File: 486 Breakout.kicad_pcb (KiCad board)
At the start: 4 copper layers, 100 x 100 mm, 51 parts, among them J1 PWR, J10 Conn_02x03_Counter_Clockwise, J11 Cache FPU, J12 Parity, J13 Bus Size Byte Enabled, J14 Bus Arbitration, J2 Not Connected, J3 Address Bus, J4 Data Bus, J5 CLK, J6 Conn_02x03_Counter_Clockwise, J7 Int, J8 Control Bus, J9 Conn_02x04_Counter_Clockwise, SW1 POWER, SW2 RESET, U1 80486, U2 7400, U3 7400

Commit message: V2 of the board
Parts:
- removed G***: LOGO, Private_lib:Fox Logo
- removed the J7 at (165.6, 117.6)
- removed the R20 at (157.8, 119.1)
- removed SW1: POWER, Button_Switch_THT:SW_NKK_G1xJP
- removed SW2: RESET, Button_Switch_THT:SW_PUSH_6mm_H5mm
- added #LOGO1: LOGO, Private_lib:Fox Logo, F.Cu at (157.2, 133.3)
- added J12: FPU, Connector_PinHeader_2.54mm:PinHeader_1x02_P2.54mm_Vertical, F.Cu at (74.9, 124.7)
- added J14: Bus Size, Connector_PinHeader_2.54mm:PinHeader_1x02_P2.54mm_Vertical, F.Cu at (74.4, 75.4)
- added R14: 10k, Resistor_THT:R_Axial_DIN0204_L3.6mm_D1.6mm_P7.62mm_Horizontal, F.Cu at (158.8, 77.0)
- C1, C10, C2, C3, C4, C5, C6, C7, C8, C9: value C -> 105
- D1: value LED_ALT -> POWER
- J11: renamed from J13; value Bus Size Byte Enabled -> Byte Enabled; footprint Connector_PinHeader_2.54mm:PinHeader_1x08_P2.54mm_Vertical -> Connector_PinHeader_2.54mm:PinHeader_1x06_P2.54mm_Vertical
- J13: renamed from J5; value CLK -> Input; footprint Connector_PinHeader_2.54mm:PinHeader_1x01_P2.54mm_Vertical -> Connector_PinHeader_2.54mm:PinHeader_1x04_P2.54mm_Vertical
- J7: renamed from J8; footprint Connector_PinHeader_2.54mm:PinHeader_1x10_P2.54mm_Vertical -> Connector_PinHeader_2.54mm:PinHeader_1x09_P2.54mm_Vertical
- J8: renamed from J11; value Cache FPU -> Cache; footprint Connector_PinHeader_2.54mm:PinHeader_1x08_P2.54mm_Vertical -> Connector_PinHeader_2.54mm:PinHeader_1x06_P2.54mm_Vertical
- R1: footprint Resistor_THT:R_Axial_DIN0204_L3.6mm_D1.6mm_P5.08mm_Horizontal -> Resistor_THT:R_Axial_DIN0204_L3.6mm_D1.6mm_P7.62mm_Horizontal
- R10: renamed from R12; footprint Resistor_THT:R_Axial_DIN0204_L3.6mm_D1.6mm_P5.08mm_Horizontal -> Resistor_THT:R_Axial_DIN0204_L3.6mm_D1.6mm_P7.62mm_Horizontal
- R11: renamed from R13; footprint Resistor_THT:R_Axial_DIN0204_L3.6mm_D1.6mm_P5.08mm_Horizontal -> Resistor_THT:R_Axial_DIN0204_L3.6mm_D1.6mm_P7.62mm_Horizontal
- R12: renamed from R14; footprint Resistor_THT:R_Axial_DIN0204_L3.6mm_D1.6mm_P5.08mm_Horizontal -> Resistor_THT:R_Axial_DIN0204_L3.6mm_D1.6mm_P7.62mm_Horizontal
- R13: renamed from R15; footprint Resistor_THT:R_Axial_DIN0204_L3.6mm_D1.6mm_P5.08mm_Horizontal -> Resistor_THT:R_Axial_DIN0204_L3.6mm_D1.6mm_P7.62mm_Horizontal
- R15: renamed from R16; footprint Resistor_THT:R_Axial_DIN0204_L3.6mm_D1.6mm_P5.08mm_Horizontal -> Resistor_THT:R_Axial_DIN0204_L3.6mm_D1.6mm_P7.62mm_Horizontal
- R16: renamed from R17; footprint Resistor_THT:R_Axial_DIN0204_L3.6mm_D1.6mm_P5.08mm_Horizontal -> Resistor_THT:R_Axial_DIN0204_L3.6mm_D1.6mm_P7.62mm_Horizontal
- R17: renamed from R18; footprint Resistor_THT:R_Axial_DIN0204_L3.6mm_D1.6mm_P5.08mm_Horizontal -> Resistor_THT:R_Axial_DIN0204_L3.6mm_D1.6mm_P7.62mm_Horizontal
- R18: renamed from R19; footprint Resistor_THT:R_Axial_DIN0204_L3.6mm_D1.6mm_P5.08mm_Horizontal -> Resistor_THT:R_Axial_DIN0204_L3.6mm_D1.6mm_P7.62mm_Horizontal
- R19: renamed from R2; footprint Resistor_THT:R_Axial_DIN0204_L3.6mm_D1.6mm_P5.08mm_Horizontal -> Resistor_THT:R_Axial_DIN0204_L3.6mm_D1.6mm_P7.62mm_Horizontal
- R2: renamed from R4; footprint Resistor_THT:R_Axial_DIN0204_L3.6mm_D1.6mm_P5.08mm_Horizontal -> Resistor_THT:R_Axial_DIN0204_L3.6mm_D1.6mm_P7.62mm_Horizontal
- R20: renamed from R3; footprint Resistor_THT:R_Axial_DIN0204_L3.6mm_D1.6mm_P5.08mm_Horizontal -> Resistor_THT:R_Axial_DIN0204_L3.6mm_D1.6mm_P7.62mm_Horizontal
- R3: renamed from R5; footprint Resistor_THT:R_Axial_DIN0204_L3.6mm_D1.6mm_P5.08mm_Horizontal -> Resistor_THT:R_Axial_DIN0204_L3.6mm_D1.6mm_P7.62mm_Horizontal
- R4: renamed from R6; footprint Resistor_THT:R_Axial_DIN0204_L3.6mm_D1.6mm_P5.08mm_Horizontal -> Resistor_THT:R_Axial_DIN0204_L3.6mm_D1.6mm_P7.62mm_Horizontal
- R5: renamed from R7; footprint Resistor_THT:R_Axial_DIN0204_L3.6mm_D1.6mm_P5.08mm_Horizontal -> Resistor_THT:R_Axial_DIN0204_L3.6mm_D1.6mm_P7.62mm_Horizontal
- R6: renamed from R8; footprint Resistor_THT:R_Axial_DIN0204_L3.6mm_D1.6mm_P5.08mm_Horizontal -> Resistor_THT:R_Axial_DIN0204_L3.6mm_D1.6mm_P7.62mm_Horizontal
- R7: renamed from R9; footprint Resistor_THT:R_Axial_DIN0204_L3.6mm_D1.6mm_P5.08mm_Horizontal -> Resistor_THT:R_Axial_DIN0204_L3.6mm_D1.6mm_P7.62mm_Horizontal
- R8: renamed from R10; footprint Resistor_THT:R_Axial_DIN0204_L3.6mm_D1.6mm_P5.08mm_Horizontal -> Resistor_THT:R_Axial_DIN0204_L3.6mm_D1.6mm_P7.62mm_Horizontal
- R9: renamed from R11; footprint Resistor_THT:R_Axial_DIN0204_L3.6mm_D1.6mm_P5.08mm_Horizontal -> Resistor_THT:R_Axial_DIN0204_L3.6mm_D1.6mm_P7.62mm_Horizontal
- U1: value 80486 -> 80486DX
- moved J6 42.6 mm to (87.9, 117.8), turned to 0 degrees
- moved J10 37.7 mm to (158.0, 97.0)
- moved R11 31.1 mm to (158.8, 73.9)
- moved R7 29.0 mm to (89.4, 140.2)
- moved R1 28.5 mm to (158.8, 70.9)
- moved R17 27.6 mm to (158.8, 83.1)
- moved C10 27.2 mm to (130.8, 124.7)
- moved U3 27.2 mm to (119.4, 124.7)
- moved R2 24.4 mm to (80.3, 81.8), turned to 180 degrees
- moved R19 24.3 mm to (158.8, 89.2)
- moved R20 24.1 mm to (158.8, 92.2)
- moved R6 23.7 mm to (89.4, 137.7)
- moved R16 22.2 mm to (158.8, 80.0)
- moved R18 21.7 mm to (158.8, 86.1)
- moved R5 18.4 mm to (89.4, 135.1)
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- renumbered J14 to J15, J9 to J2, J2 to J3, J3 to J4, J4 to J5, J12 to J9
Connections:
- net /RDY*R renamed /RDY#R
- net ADS* renamed ADS#
- net BE0* renamed BE0#
- net BE1* renamed BE1#
- net BE2* renamed BE2#
- net BE3* renamed BE3#
- net BLAST* renamed BLAST#
- net BOFF* renamed BOFF#
- net D_C* renamed D_C#
- net EADS* renamed EADS#
- net FERR* renamed FERR#
- net FLUSH* renamed FLUSH#
- net LOCK* renamed LOCK#
- net M_IO* renamed M_IO#
- net PCHK* renamed PCHK#
- net PLOCK* renamed PLOCK#
- net RDY* renamed RDY#
- net W_R* renamed W_R#
- J1 pad 1: Net-(J1-Pad1) -> +5V
- J10 pad 4: /BRDY*R -> /BRDY#R
- J2 pad 2: Net-(J9-Pad2) -> Net-(J2-Pad2)
- J2 pad 4: Net-(J9-Pad4) -> Net-(J2-Pad4)
- J2 pad 6: Net-(J9-Pad6) -> Net-(J2-Pad6)
- J2 pad 8: Net-(J9-Pad8) -> Net-(J2-Pad8)
- J6 pad 1: A20M* -> A20M#
- J6 pad 3: KEN* -> KEN#
- J6 pad 5: IGNNE* -> IGNNE#
- J7 pad 6: BRDY* -> BRDY#
- J8 pad 1: IGNNE* -> IGNNE#
- J8 pad 5: KEN* -> KEN#
- R12 pad 1: BS16* -> BS8#
- R13 pad 1: BS8* -> BS16#
- R17 pad 1: NMI -> INTR
- R18 pad 1: INTR -> NMI
- R2 pad 1: KEN* -> A20M#
- R20 pad 1: /BRDY*R -> BRDY#
- R20 pad 2: BRDY* -> /BRDY#R
- R3 pad 1: A20M* -> IGNNE#
- R4 pad 1: Net-(J9-Pad8) -> Net-(J2-Pad2)
- R5 pad 1: Net-(J9-Pad6) -> Net-(J2-Pad4)
- R6 pad 1: Net-(J9-Pad4) -> Net-(J2-Pad6)
- R7 pad 1: Net-(J9-Pad2) -> Net-(J2-Pad8)
- R9 pad 1: IGNNE* -> KEN#
- U1 pad A15: IGNNE* -> IGNNE#
- U1 pad C17: BS16* -> BS16#
- U1 pad D15: A20M* -> A20M#
- U1 pad D16: BS8* -> BS8#
- U1 pad F15: KEN* -> KEN#
- U1 pad H15: BRDY* -> BRDY#
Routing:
- net IGNNE*: track 139.2 -> 0.00 mm
- net A24: track 210.1 -> 72.5 mm, vias 2 -> 1
- net KEN#: track 0.00 -> 119.4 mm
- net KEN*: track 115.1 -> 0.00 mm, vias 2 -> 0
- net A20M#: track 0.00 -> 114.8 mm, vias 0 -> 3
- net BRDY*: track 109.0 -> 0.00 mm
- net A20M*: track 107.7 -> 0.00 mm, vias 2 -> 0
- net A30: track 77.6 -> 170.7 mm, vias 1 -> 3
- net IGNNE#: track 0.00 -> 86.1 mm
- net A29: track 193.8 -> 110.0 mm
- net A18: track 133.4 -> 52.8 mm, vias 2 -> 0
- net LOCK#: track 41.1 -> 109.9 mm, vias 0 -> 1
- net BS8#: track 0.00 -> 67.5 mm
- net BS16#: track 0.00 -> 64.5 mm
- net A28: track 90.3 -> 152.6 mm
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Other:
- board text added: "486-DX Breakout Board V2.0 Created by Fox Cutter"
- board text added: "A0 is valid when ~BS8~ is asserted."
- board text added: "A1 is valid when ~BS8~ or ~BS16~ are asserted."
- board text added: "A15"
- board text added: "A23"
- board text added: "A3 (TCK) A10 A12 A13 A14 (TDI) B10 B12 B13 B14 (TMS) B16 (TDO) C10 C11 (~UP~) C12 C13 G15 R17 S4"
- board text added: "A7"
- board text added: "AHOLD ~EADS ~KEN ~FLUSH PWT PCD"
- board text added: "BREQ HOLD HLDA ~BOFF"
- board text added: "CLK RESET INTR NMI"
- board text added: "D15"
- board text added: "D23"
- board text added: "D7"
- board text added: "DP0 DP1 DP2 DP3 ~PCHK"
- board text added: "M/~IO D/~C W/~R ~ADS ~RDY ~BRDY ~BLAST ~LOCK ~PLOCK"
- board text added: "Pull Low Pull High"
- board text added: "when ~BS16~ is asserted."
- board text added: "~A20M ~KEN ~IGNNE"
- board text added: "~BE0 ~BE1 ~BE2 ~BE3 ~BLE ~BHE"
- board text added: "~BHE~ and ~BLE~ are valid"
- board text added: "~BS8 ~BS16"
- board text added: "~IGNNE ~FERR"
- board text added: "~RDY ~BRDY"
- board text removed: "486-DX Breakout Board V1.0 Created by Fox Cutter"
- board text removed: "A0 is valid when BS8# is asserted. A1 is valid when BS8# or BS16# are asserted."
- board text removed: "A3 (TCK) A10 A12 A13 A14 (TDI) B10 B12 B13 B14 (TMS) B16 (TDO) C10 C11 (UP#) C12 C13 G15 R17 S4"
- board text removed: "BE0# BE1# BE2# BE3# BLE# BHE# BS8# BS16#"
- board text removed: "BHE# and BLE# are valid when BS16# is asserted."
- board text removed: "BREQ HOLD HLDA BOFF#"
- board text removed: "DP0 DP1 DP2 DP3 PCHK#"
- board text removed: "IGNNE# FERR# AHOLD EADS# KEN# FLUSH# PWT PCD"
- board text removed: "IGNNE# KEN# A20M#"
- board text removed: "INTR NMI"
- board text removed: "M/IO# D/C# W/R# ADS# RDY# BRDY# BLAST# LOCK# PLOCK# RESET"
- board text removed: "Pull Low Float Pull High"
- board text removed: "RDY# BRDY#"
- board text removed: "ZIF Socket"

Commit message: * Update to Kicad 6
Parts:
- J13: footprint Connector_PinHeader_2.54mm:PinHeader_1x04_P2.54mm_Vertical -> Connector_PinHeader_2.54mm:PinHeader_1x06_P2.54mm_Vertical
- J7: footprint Connector_PinHeader_2.54mm:PinHeader_1x09_P2.54mm_Vertical -> Connector_PinHeader_2.54mm:PinHeader_1x07_P2.54mm_Vertical
- U1: footprint 486:PGA169 -> 486 Breakout:PGA169
- moved J10 19.4 mm to (158.1, 77.7)
- moved R11 17.1 mm to (158.4, 91.0)
- moved R14 17.1 mm to (158.4, 94.1)
- moved R16 17.1 mm to (158.4, 97.1)
- moved R17 17.1 mm to (158.4, 100.2)
- moved R18 17.1 mm to (158.4, 103.2)
- moved R19 17.1 mm to (158.4, 106.3)
- moved R20 17.1 mm to (158.4, 109.3)
- moved U2 6.67 mm to (110.3, 124.9)
- moved U3 6.67 mm to (126.1, 124.9)
- moved C10 6.67 mm to (137.5, 124.9)
- moved C9 6.67 mm to (121.5, 124.9)
- moved J7 3.59 mm to (165.7, 90.3)
- moved J6 2.17 mm to (88.0, 115.7)
- moved J15 1.90 mm to (165.7, 110.5)
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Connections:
- J12 pad 1: PWT -> IGNNE#
- J12 pad 2: PCD -> FERR#
- J13 pad 3: INTR -> RDY#
- J13 pad 4: NMI -> BRDY#
- J7 pad 5: RDY# -> BLAST#
- J7 pad 6: BRDY# -> LOCK#
- J7 pad 7: BLAST# -> PLOCK#
- J8 pad 1: IGNNE# -> AHOLD
- J8 pad 2: FERR# -> EADS#
- J8 pad 3: AHOLD -> KEN#
- J8 pad 4: EADS# -> FLUSH#
- J8 pad 5: KEN# -> PWT
- J8 pad 6: FLUSH# -> PCD
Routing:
- net A31: track 189.7 -> 92.8 mm
- net A27: track 77.3 -> 165.1 mm, vias 0 -> 1
- net A30: track 170.7 -> 90.9 mm, vias 3 -> 0
- net NMI: track 68.1 -> 133.4 mm, vias 0 -> 8
- net A11: track 93.1 -> 28.3 mm, vias 5 -> 2
- net A18: track 52.8 -> 115.2 mm, vias 0 -> 6
- net INTR: track 71.9 -> 133.8 mm, vias 0 -> 3
- net A26: track 79.1 -> 139.1 mm, vias 0 -> 3
- net A9: track 40.0 -> 99.8 mm, vias 2 -> 11
- net A23: track 76.3 -> 132.7 mm, vias 2 -> 5
- net D10: track 55.6 -> 108.7 mm
- net LOCK#: track 109.9 -> 57.8 mm, vias 1 -> 2
- net NC1: track 33.0 -> 85.0 mm, vias 0 -> 2
- net A5: track 31.2 -> 82.3 mm, vias 1 -> 5
- net A29: track 110.0 -> 160.9 mm, vias 1 -> 6
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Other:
- net class +5V removed
- net class Default removed
- net class GND removed
- board text added: "A0 is valid when ~{BS8} is asserted."
- board text added: "A1 is valid when ~{BS8} or ~{BS16} are asserted."
- board text added: "A3 (TCK) A10 A12 A13 A14 (TDI) B10 B12 B13 B14 (TMS) B16 (TDO) C10 C11 (~{UP}) C12 C13 G15 R17 S4"
- board text added: "AHOLD ~{EADS} ~{KEN} ~{FLUSH} PWT PCD"
- board text added: "BREQ HOLD HLDA ~{BOFF}"
- board text added: "CLK RESET ~{RDY} ~{BRDY} INTR NMI"
- board text added: "DP0 DP1 DP2 DP3 ~{PCHK}"
- board text added: "M/~{IO} D/~{C} W/~{R} ~{ADS} ~{BLAST} ~{LOCK} ~{PLOCK}"
- board text added: "when ~{BS16} is asserted."
- board text added: "~{A20M} ~{KEN} ~{IGNNE}"
- board text added: "~{BE0} ~{BE1} ~{BE2} ~{BE3} ~{BLE} ~{BHE}"
- board text added: "~{BHE} and ~{BLE} are valid"
- board text added: "~{BS8} ~{BS16}"
- board text added: "~{IGNNE} ~{FERR}"
- board text added: "~{RDY} ~{BRDY}"
- board text removed: "A0 is valid when ~BS8~ is asserted."
- board text removed: "A1 is valid when ~BS8~ or ~BS16~ are asserted."
- board text removed: "A3 (TCK) A10 A12 A13 A14 (TDI) B10 B12 B13 B14 (TMS) B16 (TDO) C10 C11 (~UP~) C12 C13 G15 R17 S4"
- board text removed: "AHOLD ~EADS ~KEN ~FLUSH PWT PCD"
- board text removed: "BREQ HOLD HLDA ~BOFF"
- board text removed: "CLK RESET INTR NMI"
- board text removed: "DP0 DP1 DP2 DP3 ~PCHK"
- board text removed: "M/~IO D/~C W/~R ~ADS ~RDY ~BRDY ~BLAST ~LOCK ~PLOCK"
- board text removed: "when ~BS16~ is asserted."
- board text removed: "~A20M ~KEN ~IGNNE"
- board text removed: "~BE0 ~BE1 ~BE2 ~BE3 ~BLE ~BHE"
- board text removed: "~BHE~ and ~BLE~ are valid"
- board text removed: "~BS8 ~BS16"
- board text removed: "~IGNNE ~FERR"
- board text removed: "~RDY ~BRDY"

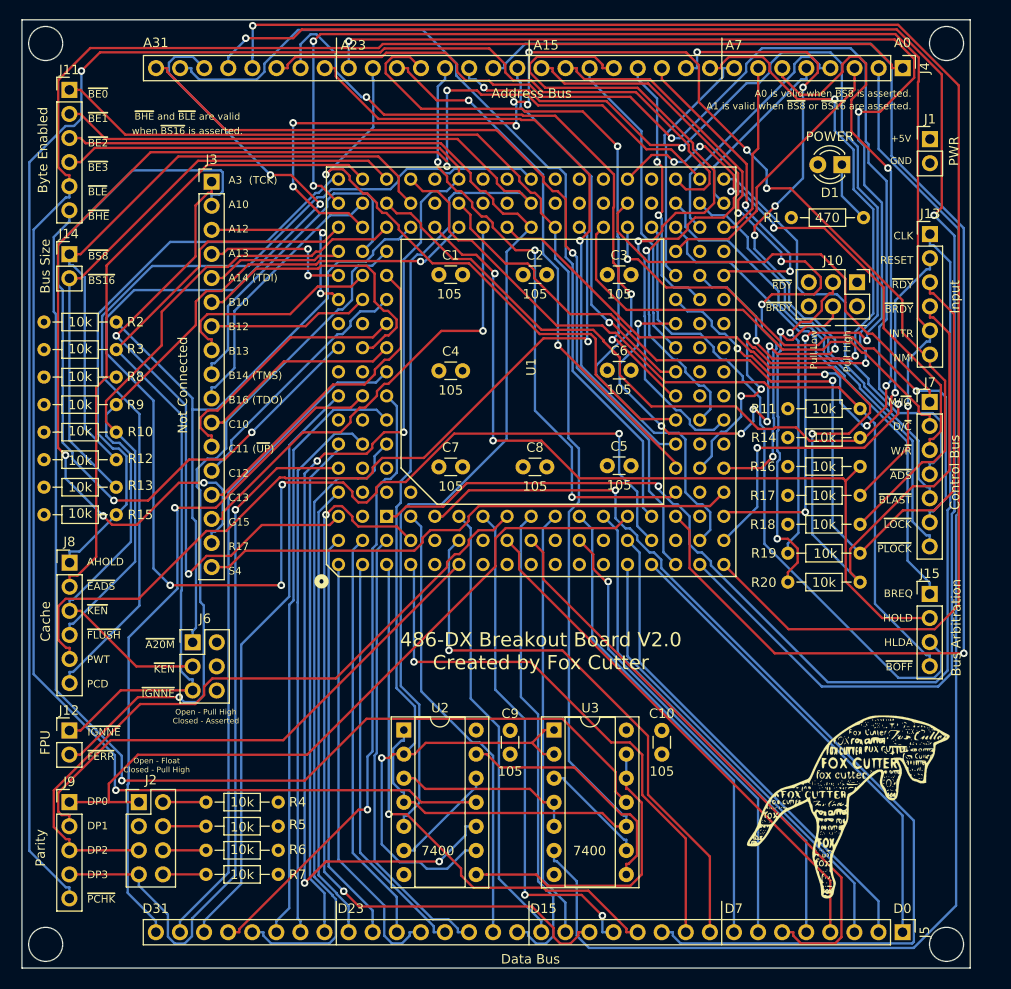
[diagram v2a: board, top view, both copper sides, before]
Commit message: Updating the 486 Breakout Board
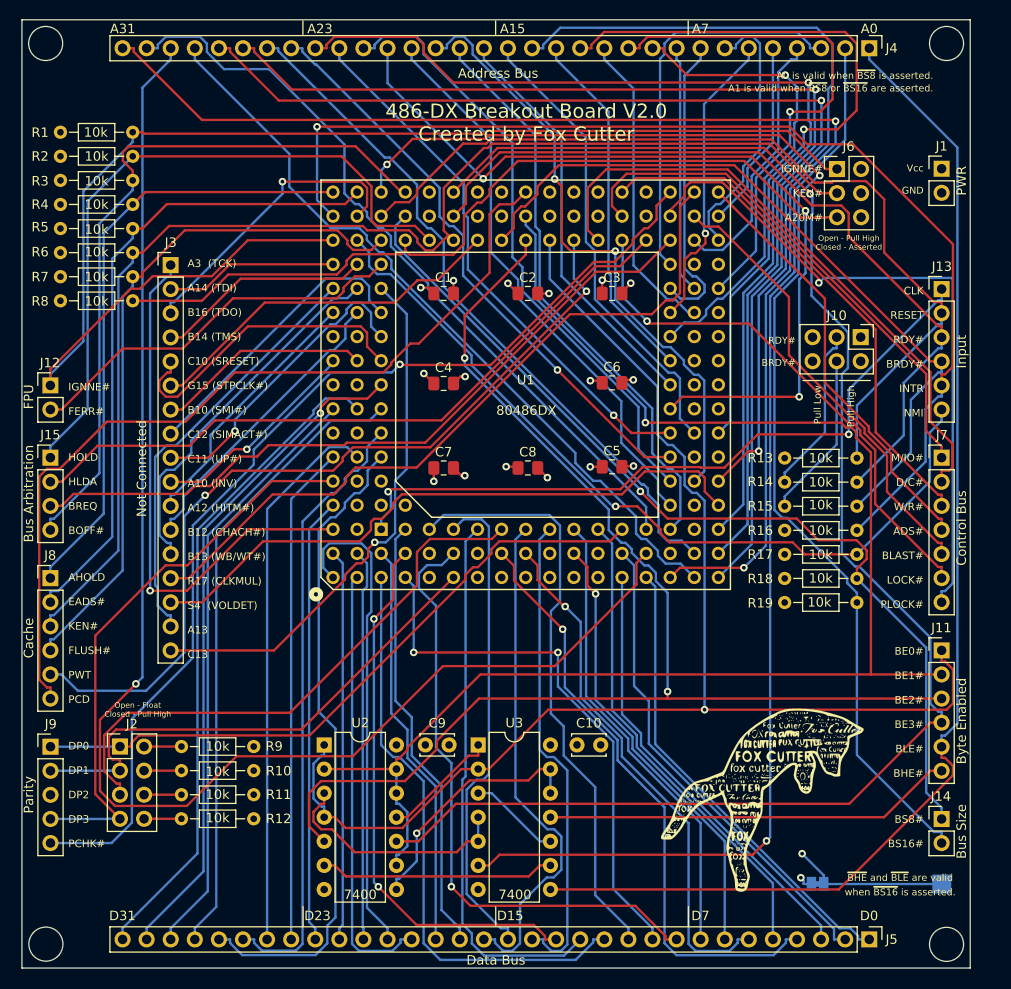
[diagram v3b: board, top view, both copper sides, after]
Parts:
- removed D1: POWER, LED_THT:LED_D3.0mm
- removed R20: 10k, Resistor_THT:R_Axial_DIN0204_L3.6mm_D1.6mm_P7.62mm_Horizontal
- added JP1: Vcc to J1, Jumper:SolderJumper-2_P1.3mm_Bridged_Pad1.0x1.5mm, B.Cu at (153.9, 141.1)
- added TP1: +5V, TestPoint:TestPoint_Pad_2.0x2.0mm, B.Cu at (167.0, 141.1)
- C1, C2, C3, C4, C5, C6, C7, C8: footprint Capacitor_THT:C_Disc_D3.0mm_W1.6mm_P2.50mm -> Capacitor_SMD:C_0805_2012Metric_Pad1.18x1.45mm_HandSolder
- C10, C9: footprint Capacitor_THT:C_Disc_D3.0mm_W1.6mm_P2.50mm -> Capacitor_THT:C_Disc_D3.4mm_W2.1mm_P2.50mm
- R1: value 470 -> 10k
- U2, U3: footprint Package_DIP:DIP-14_W7.62mm_Socket -> Package_DIP:DIP-14_W7.62mm
- moved J14 109.6 mm to (167.0, 134.3)
- moved J11 109.3 mm to (167.0, 116.5)
- moved J15 93.8 mm to (73.0, 96.2)
- moved R1 85.2 mm to (74.1, 61.9), turned to 0 degrees
- moved J6 84.3 mm to (155.9, 65.7)
- moved R11 82.3 mm to (86.8, 131.7), turned to 0 degrees
- moved R13 78.2 mm to (158.1, 96.2)
- moved R15 78.1 mm to (158.1, 101.3)
- moved R7 64.9 mm to (74.1, 77.1)
- moved R6 64.9 mm to (74.1, 74.6)
- moved R5 64.9 mm to (74.1, 72.0)
- moved R4 63.5 mm to (81.7, 69.5), turned to 180 degrees
- moved R12 38.5 mm to (86.8, 134.3), turned to 0 degrees
- moved R9 36.7 mm to (86.8, 126.6), turned to 0 degrees
- moved J12 36.4 mm to (73.0, 88.6)
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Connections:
- net NC0 renamed NC_A3
- C1 pad 2: +5V -> VCC
- C10 pad 1: +5V -> VCC
- C2 pad 2: +5V -> VCC
- C3 pad 2: +5V -> VCC
- C4 pad 2: +5V -> VCC
- C5 pad 2: +5V -> VCC
- C6 pad 2: +5V -> VCC
- C7 pad 2: +5V -> VCC
- C8 pad 2: +5V -> VCC
- C9 pad 1: +5V -> VCC
- J1 pad 1: +5V -> VCC
- J10 pad 1: +5V -> VCC
- J10 pad 2: +5V -> VCC
- J15 pad 1: BREQ -> HOLD
- J15 pad 2: HOLD -> HLDA
- J15 pad 3: HLDA -> BREQ
- J3 pad 10: NC9 -> NC_A10
- J3 pad 11: NC10 -> NC_A12
- J3 pad 12: NC11 -> NC_B12
- J3 pad 13: NC12 -> NC_B13
- J3 pad 14: NC13 -> NC_R17
- J3 pad 15: NC14 -> NC_S4
- J3 pad 16: NC15 -> NC_A13
- J3 pad 17: NC16 -> NC_C13
- J3 pad 2: NC1 -> NC_A14
- J3 pad 3: NC2 -> NC_B16
- J3 pad 4: NC3 -> NC_B14
- J3 pad 5: NC4 -> NC_C10
- J3 pad 6: NC5 -> NC_G15
- J3 pad 7: NC6 -> NC_B10
- J3 pad 8: NC7 -> NC_C12
- J3 pad 9: NC8 -> NC_C11
- J6 pad 1: A20M# -> IGNNE#
- J6 pad 5: IGNNE# -> A20M#
- R1 pad 1: Net-(D1-Pad1) -> VCC
- R1 pad 2: GND -> IGNNE#
- R10 pad 1: FLUSH# -> Net-(J2-Pad4)
- R10 pad 2: +5V -> VCC
- R11 pad 1: BOFF# -> Net-(J2-Pad6)
- R11 pad 2: +5V -> VCC
- R12 pad 1: BS8# -> Net-(J2-Pad8)
- R12 pad 2: +5V -> VCC
- R13 pad 1: BS16# -> RESET
- R13 pad 2: +5V -> GND
- R14 pad 1: RESET -> RDY#
- R14 pad 2: GND -> /RDY#R
- R15 pad 1: AHOLD -> BRDY#
- R15 pad 2: GND -> /BRDY#R
- R16 pad 1: HOLD -> INTR
- R17 pad 1: INTR -> NMI
- R18 pad 1: NMI -> VCC
- R18 pad 2: GND -> BS8#
- R19 pad 1: RDY# -> VCC
- R19 pad 2: /RDY#R -> BS16#
- R2 pad 1: A20M# -> HOLD
- R2 pad 2: +5V -> GND
- R3 pad 1: IGNNE# -> VCC
- R3 pad 2: +5V -> BOFF#
- R4 pad 1: Net-(J2-Pad2) -> AHOLD
- R4 pad 2: +5V -> GND
- R5 pad 1: Net-(J2-Pad4) -> VCC
- R5 pad 2: +5V -> EADS#
- R6 pad 1: Net-(J2-Pad6) -> VCC
- R6 pad 2: +5V -> KEN#
- R7 pad 1: Net-(J2-Pad8) -> VCC
- R7 pad 2: +5V -> FLUSH#
- R8 pad 1: EADS# -> VCC
- R8 pad 2: +5V -> A20M#
- R9 pad 1: KEN# -> Net-(J2-Pad2)
- R9 pad 2: +5V -> VCC
- U1 pad A10: NC1 -> NC_A10
- U1 pad A12: NC2 -> NC_A12
- U1 pad A13: NC3 -> NC_A13
- U1 pad A14: NC4 -> NC_A14
- U1 pad B10: NC5 -> NC_B10
- U1 pad B11: +5V -> VCC
- U1 pad B12: NC6 -> NC_B12
- U1 pad B13: NC7 -> NC_B13
- U1 pad B14: NC8 -> NC_B14
- U1 pad B16: NC9 -> NC_B16
- U1 pad B7: +5V -> VCC
- U1 pad B9: +5V -> VCC
- U1 pad C10: NC10 -> NC_C10
- U1 pad C11: NC11 -> NC_C11
- U1 pad C12: NC12 -> NC_C12
- U1 pad C13: NC13 -> NC_C13
- U1 pad C4: +5V -> VCC
- U1 pad C5: +5V -> VCC
- U1 pad D4: (no net) -> unconnected-(U1-PadD4)
- U1 pad E16: +5V -> VCC
- U1 pad E2: +5V -> VCC
- U1 pad G15: NC14 -> NC_G15
- U1 pad G16: +5V -> VCC
- U1 pad G2: +5V -> VCC
- U1 pad H16: +5V -> VCC
- U1 pad K16: +5V -> VCC
- U1 pad K2: +5V -> VCC
- U1 pad L16: +5V -> VCC
- U1 pad M16: +5V -> VCC
- U1 pad M2: +5V -> VCC
- U1 pad P16: +5V -> VCC
- U1 pad R10: +5V -> VCC
- U1 pad R11: +5V -> VCC
- U1 pad R14: +5V -> VCC
- U1 pad R17: NC15 -> NC_R17
- U1 pad R3: +5V -> VCC
- U1 pad R6: +5V -> VCC
- U1 pad R8: +5V -> VCC
- U1 pad R9: +5V -> VCC
- U1 pad S4: NC16 -> NC_S4
- U2 pad 11: BLE# -> Net-(U2-Pad11)
- U2 pad 12: Net-(U2-Pad12) -> BE1#
- U2 pad 13: Net-(U2-Pad13) -> BE1#
- U2 pad 14: +5V -> VCC
- U2 pad 6: Net-(U2-Pad12) -> Net-(U2-Pad6)
- U3 pad 1: BE1# -> Net-(U2-Pad11)
- U3 pad 10: BE0# -> Net-(U3-Pad10)
- U3 pad 14: +5V -> VCC
- U3 pad 2: BE1# -> BE0#
- U3 pad 3: Net-(U3-Pad3) -> Net-(U3-Pad10)
- U3 pad 8: Net-(U2-Pad13) -> BLE#
- U3 pad 9: Net-(U3-Pad3) -> Net-(U2-Pad6)
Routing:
- net NC15: track 136.6 -> 0.00 mm, vias 5 -> 0
- net A28: track 176.6 -> 81.3 mm, vias 2 -> 0
- net A17: track 148.1 -> 61.1 mm, vias 1 -> 0
- net NC1: track 85.0 -> 0.00 mm, vias 2 -> 0
- net BLE#: track 211.4 -> 129.6 mm, vias 1 -> 0
- net BHE#: track 124.6 -> 43.3 mm, vias 1 -> 0
- net NC_R17: track 0.00 -> 77.7 mm
- net BS16#: track 63.5 -> 132.4 mm, vias 0 -> 2
- net NC_S4: track 0.00 -> 66.6 mm
- net PCHK#: track 171.0 -> 110.4 mm
- net IGNNE#: track 84.1 -> 143.6 mm
- net NC16: track 57.9 -> 0.00 mm
- net +5V: track 0.00 -> 57.8 mm, vias 0 -> 1
- net NC_C13: track 0.00 -> 57.0 mm, vias 0 -> 1
- net A5: track 82.3 -> 31.7 mm, vias 5 -> 1
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- added copper zone on In1.Cu, net VCC
- removed copper zone on In1.Cu, net +5V
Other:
- board text added: "A3 (TCK) A14 (TDI) B16 (TDO) B14 (TMS) C10 (SRESET) G15 (STPCLK#) B10 (SMI#) C12 (SIMACT#) C11 (UP#) A10 (INV) A12 (HITM#) B12 (CHACH#) B13 (WB/WT#) R17 (CLKMUL) S4 (VOLDET) A13 C13"
- board text added: "AHOLD EADS# KEN# FLUSH# PWT PCD"
- board text added: "BE0# BE1# BE2# BE3# BLE# BHE#"
- board text added: "BS8# BS16#"
- board text added: "CLK RESET RDY# BRDY# INTR NMI"
- board text added: "DP0 DP1 DP2 DP3 PCHK#"
- board text added: "HOLD HLDA BREQ BOFF#"
- board text added: "IGNNE# FERR#"
- board text added: "IGNNE# KEN# A20M#"
- board text added: "M/IO# D/C# W/R# ADS# BLAST# LOCK# PLOCK#"
- board text added: "RDY# BRDY#"
- board text added: "Vcc GND"
- board text removed: "+5V GND"
- board text removed: "A3 (TCK) A10 A12 A13 A14 (TDI) B10 B12 B13 B14 (TMS) B16 (TDO) C10 C11 (~{UP}) C12 C13 G15 R17 S4"
- board text removed: "AHOLD ~{EADS} ~{KEN} ~{FLUSH} PWT PCD"
- board text removed: "BREQ HOLD HLDA ~{BOFF}"
- board text removed: "CLK RESET ~{RDY} ~{BRDY} INTR NMI"
- board text removed: "DP0 DP1 DP2 DP3 ~{PCHK}"
- board text removed: "M/~{IO} D/~{C} W/~{R} ~{ADS} ~{BLAST} ~{LOCK} ~{PLOCK}"
- board text removed: "~{A20M} ~{KEN} ~{IGNNE}"
- board text removed: "~{BE0} ~{BE1} ~{BE2} ~{BE3} ~{BLE} ~{BHE}"
- board text removed: "~{BS8} ~{BS16}"
- board text removed: "~{IGNNE} ~{FERR}"
- board text removed: "~{RDY} ~{BRDY}"
